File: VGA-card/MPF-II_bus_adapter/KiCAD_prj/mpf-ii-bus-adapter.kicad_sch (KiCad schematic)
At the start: 4 parts, among them J1 Bus_Apple_II_Card_Side, J2 Bus_Apple_II_Computer_Side, J3 DEVSEL_sel

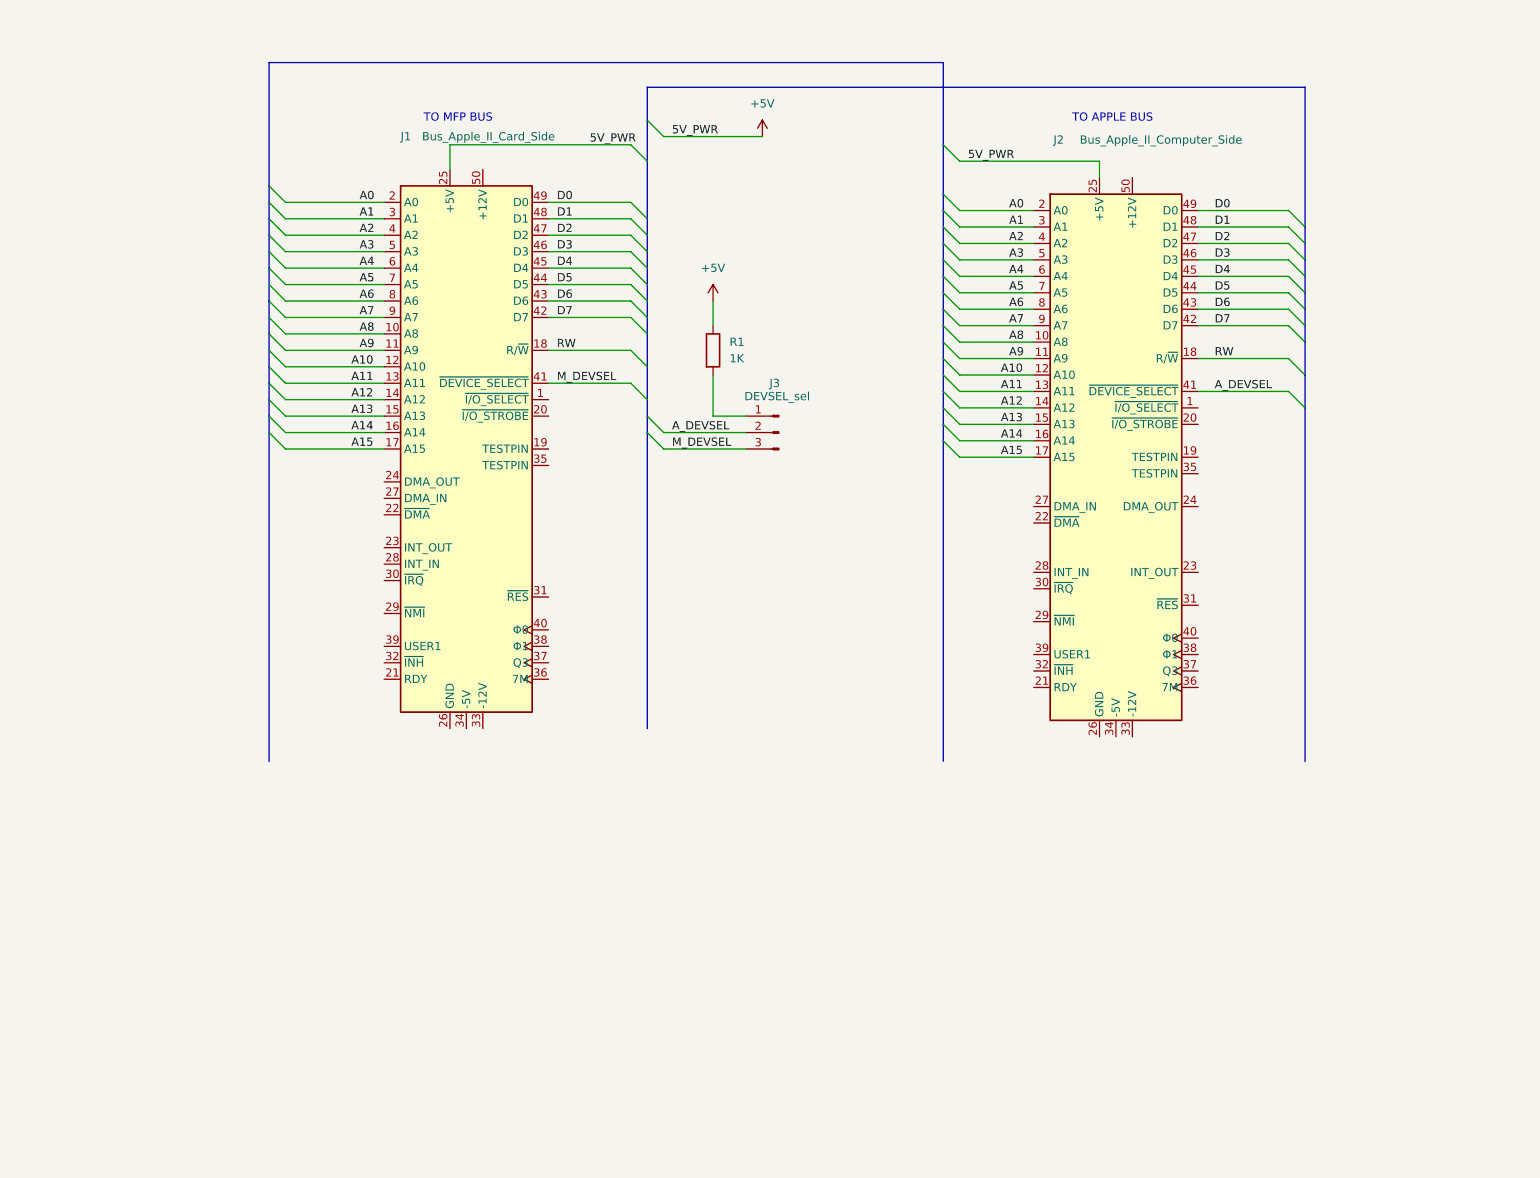
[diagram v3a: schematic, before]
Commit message: Clock signals added
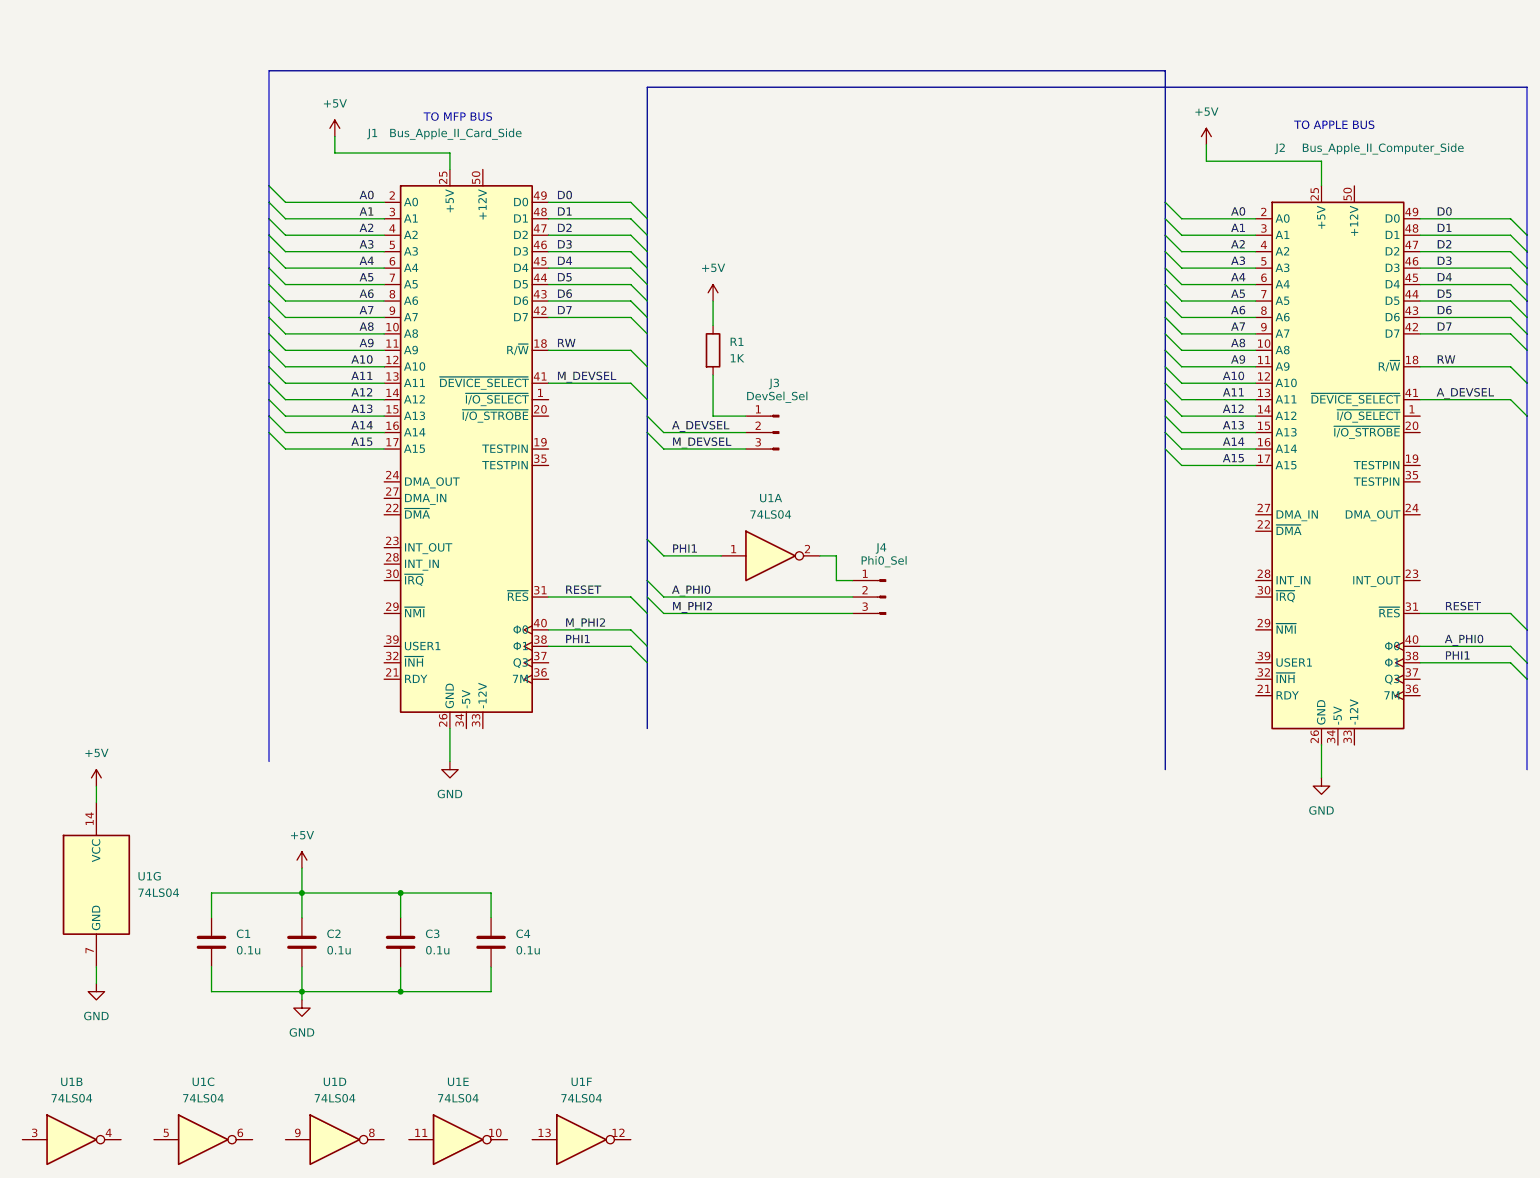
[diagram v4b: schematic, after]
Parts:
- added C1, C2, C3, C4: 0.1u, Capacitor_THT:C_Disc_D4.3mm_W1.9mm_P5.00mm, symbol Device:C
- added J4: Phi0_Sel, Connector_PinHeader_2.54mm:PinHeader_1x03_P2.54mm_Vertical, symbol Connector:Conn_01x03_Pin
- added U1: 74LS04, Package_DIP:DIP-14_W7.62mm, symbol 74xx:74LS04
- J3: value DEVSEL_sel -> DevSel_Sel
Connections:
- net +5V: now also C1.1, C2.1, C3.1, C4.1, U1.14 (VCC)
- net GND: now reaches J2.26 (GND)
- net GND: now also J1.26 (GND), C1.2, C2.2, C3.2, C4.2, U1.7 (GND)
- net RESET: now reaches J2.31 (~{RES})
- net RESET: now also J1.31 (~{RES})
- net PHI1: now reaches J2.38 (Φ1)
- net PHI1: now also J1.38 (Φ1), U1.1
- net A_PHI0: now reaches J2.40 (Φ0)
- net A_PHI0: now also J4.2 (Pin_2)
- net M_PHI2: now reaches J1.40 (Φ0)
- net M_PHI2: now also J4.3 (Pin_3)
- new net: J4.1 (Pin_1), U1.2
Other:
- moved on the sheet: J2

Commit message: Schematics updated
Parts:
- added J5: -12V_Selection, Connector_PinHeader_2.54mm:PinHeader_1x02_P2.54mm_Vertical, symbol Connector:Conn_01x02_Pin
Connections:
- net -12V: now reaches J2.33 (-12V)
- net -12V: now also J5.2 (Pin_2)
- net -5V: now reaches J2.34 (-5V)
- net -5V: now also J1.34 (-5V)
- net +12V: now reaches J2.50 (+12V)
- net +12V: now also J1.50 (+12V)
- net at J1.33 (-12V): now also J5.1 (Pin_1)

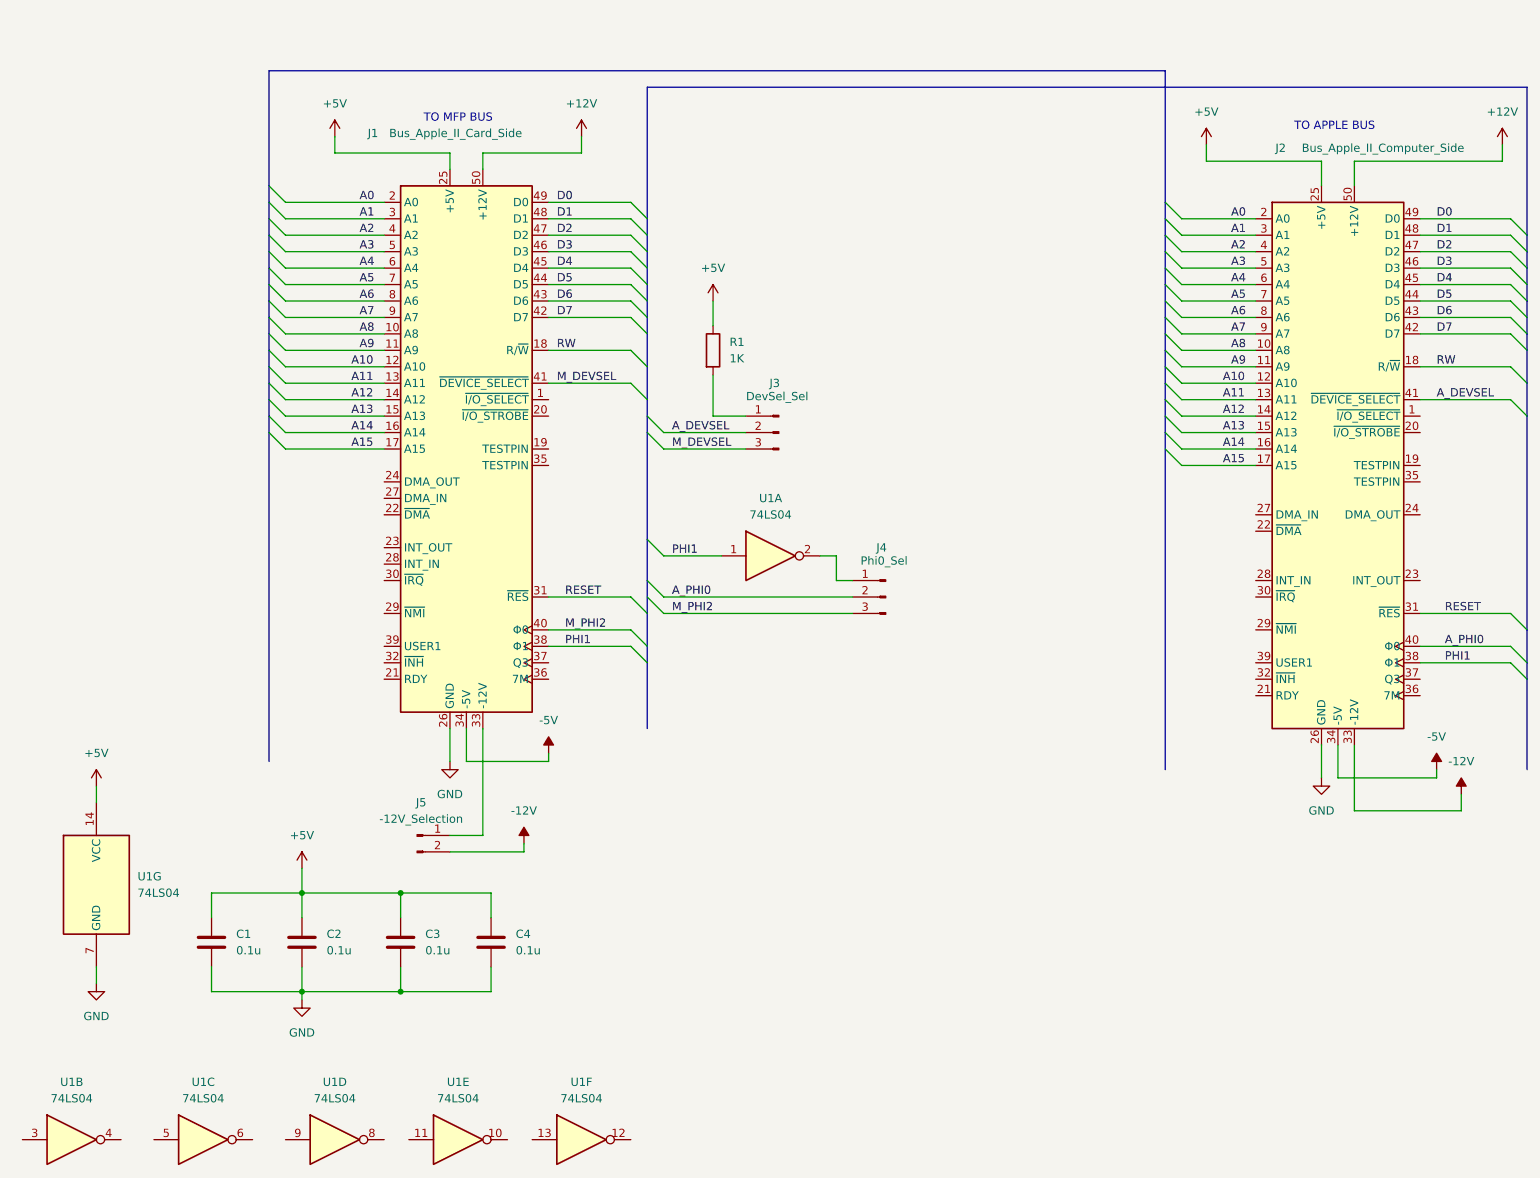
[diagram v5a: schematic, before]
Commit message: KiCAD schematics updated
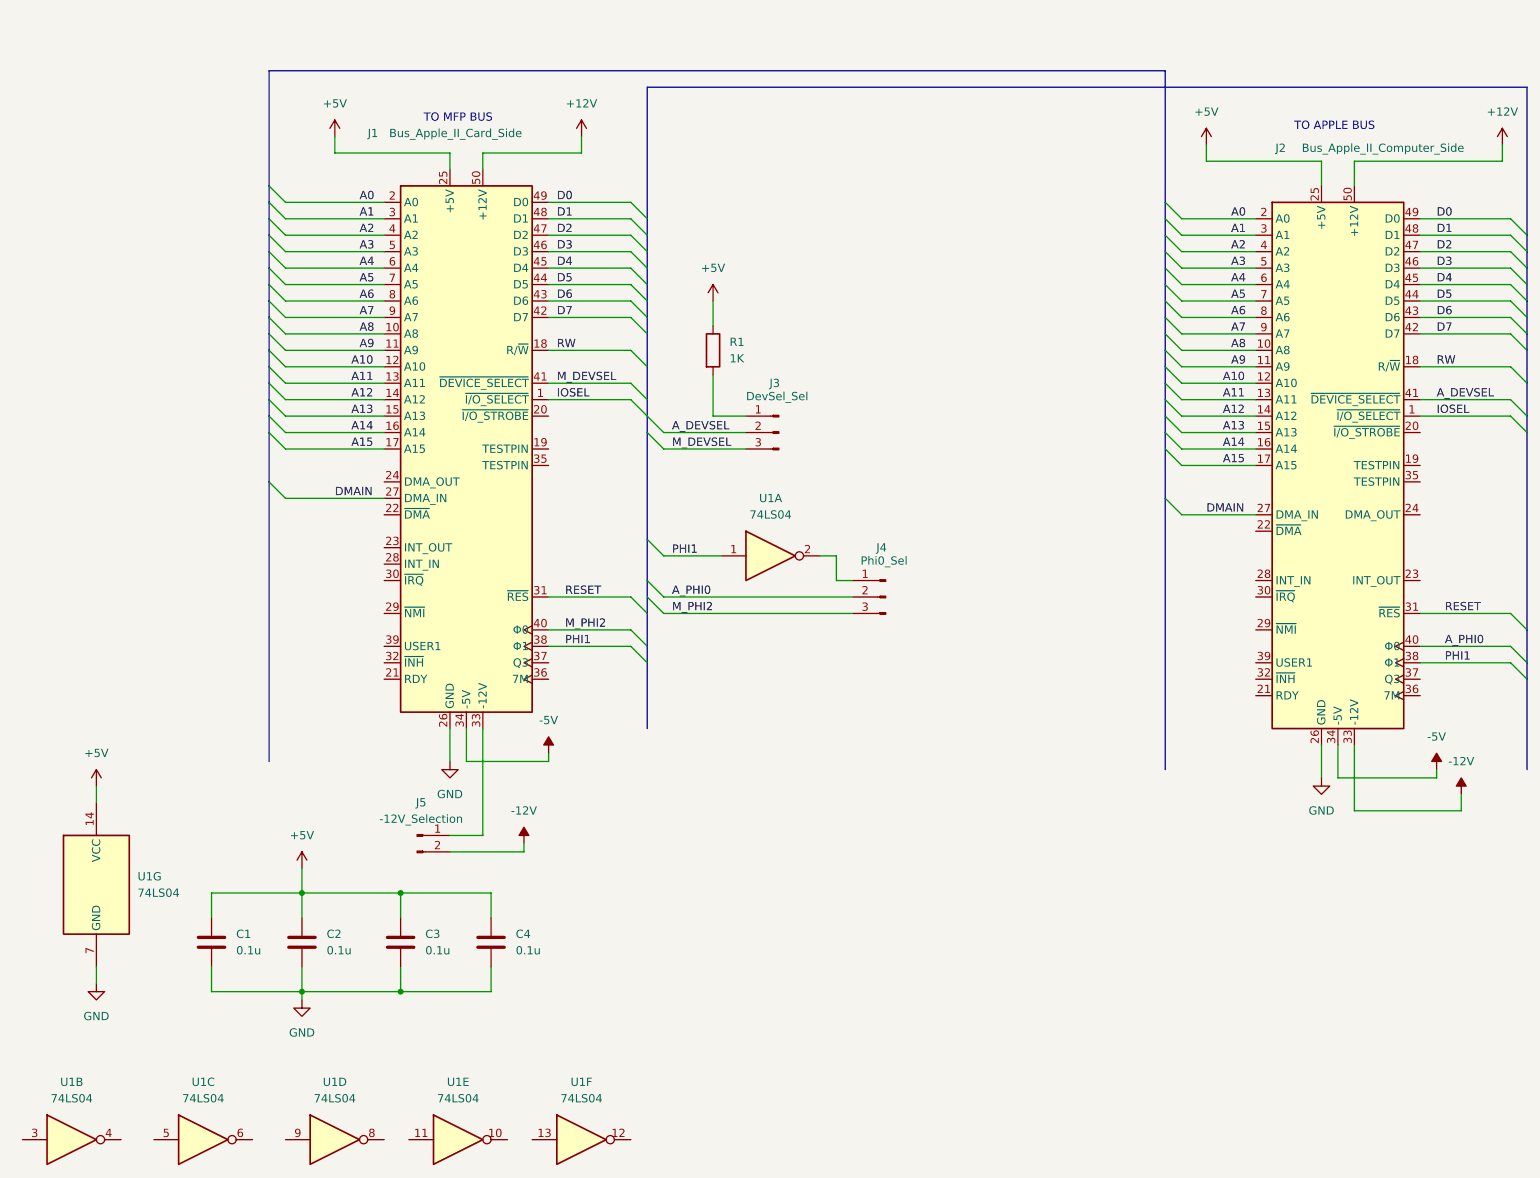
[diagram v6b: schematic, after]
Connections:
- net IOSEL: now reaches J2.1 (~{I/O_SELECT})
- net IOSEL: now also J1.1 (~{I/O_SELECT})
- net DMAIN: now reaches J2.27 (DMA_IN)
- net DMAIN: now also J1.27 (DMA_IN)
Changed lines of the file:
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@@
 	(title_block
 		(title "Microprofessor-II Bus Adapter Board")
-		(date "2024-07-19")
+		(date "2024-07-20")
 		(rev "0.1")
 		(comment 1 "Licensed under CERN-OHL-P V2.0 (https://ohwr.org/cern_ohl_p_v2.txt)")
@@
 	)
 	(bus_entry
+		(at 53.34 85.09)
+		(size 2.54 2.54)
+		(stroke
+			(width 0)
+			(type default)
+		)
+	)
+	(bus_entry
 		(at 53.34 44.45)
 		(size 2.54 2.54)
@@
 	)
 	(bus_entry
+		(at 191.77 87.63)
+		(size 2.54 2.54)
+		(stroke
+			(width 0)
+			(type default)
+		)
+	)
+	(bus_entry
 		(at 53.34 77.47)
 		(size 2.54 2.54)
@@
 	)
 	(bus_entry
+		(at 109.22 72.39)
+		(size 2.54 2.54)
+		(stroke
+			(width 0)
+			(type default)
+		)
+	)
+	(bus_entry
 		(at 53.34 67.31)
 		(size 2.54 2.54)
@@
 	)
 	(bus_entry
+		(at 245.11 74.93)
+		(size 2.54 2.54)
+		(stroke
+			(width 0)
+			(type default)
+		)
+	)
+	(bus_entry
 		(at 53.34 49.53)
 		(size 2.54 2.54)
@@
 	(bus
 		(pts
-			(xy 53.34 77.47) (xy 53.34 128.27)
+			(xy 53.34 77.47) (xy 53.34 85.09)
 		)
 		(stroke
@@
 		)
 	)
+	(bus
+		(pts
+			(xy 191.77 87.63) (xy 191.77 129.54)
+		)
+		(stroke
+			(width 0)
+			(type default)
+		)
+	)
 	(wire
 		(pts
@@
 		)
 	)
+	(wire
+		(pts
+			(xy 55.88 87.63) (xy 71.12 87.63)
+		)
+		(stroke
+			(width 0)
+			(type default)
+		)
+	)
 	(bus
 		(pts
@@
 	(wire
 		(pts
+			(xy 231.14 74.93) (xy 245.11 74.93)
+		)
+		(stroke
+			(width 0)
+			(type default)
+		)
+	)
+	(wire
+		(pts
 			(xy 44.45 148.59) (xy 58.42 148.59)
 		)
@@
 	(bus
 		(pts
-			(xy 191.77 80.01) (xy 191.77 129.54)
+			(xy 191.77 80.01) (xy 191.77 87.63)
 		)
 		(stroke
@@
 		)
 	)
+	(bus
+		(pts
+			(xy 247.65 77.47) (xy 247.65 107.95)
+		)
+		(stroke
+			(width 0)
+			(type default)
+		)
+	)
 	(wire
 		(pts
@@
 		)
 	)
+	(bus
+		(pts
+			(xy 53.34 85.09) (xy 53.34 128.27)
+		)
+		(stroke
+			(width 0)
+			(type default)
+		)
+	)
 	(wire
 		(pts
@@
 	(wire
 		(pts
+			(xy 96.52 72.39) (xy 109.22 72.39)
+		)
+		(stroke
+			(width 0)
+			(type default)
+		)
+	)
+	(wire
+		(pts
 			(xy 58.42 148.59) (xy 58.42 152.4)
 		)
@@
 	(wire
 		(pts
+			(xy 194.31 90.17) (xy 205.74 90.17)
+		)
+		(stroke
+			(width 0)
+			(type default)
+		)
+	)
+	(wire
+		(pts
 			(xy 194.31 82.55) (xy 205.74 82.55)
 		)
@@
 	(bus
 		(pts
-			(xy 247.65 74.93) (xy 247.65 107.95)
+			(xy 247.65 74.93) (xy 247.65 77.47)
 		)
 		(stroke
@@
 		)
 	)
+	(label "DMAIN"
+		(at 198.12 90.17 0)
+		(fields_autoplaced yes)
+		(effects
+			(font
+				(size 1.27 1.27)
+			)
+			(justify left bottom)
+		)
+	)
 	(label "A13"
 		(at 200.66 77.47 0)
@@
 		)
 	)
+	(label "DMAIN"
+		(at 63.5 87.63 0)
+		(fields_autoplaced yes)
+		(effects
+			(font
+				(size 1.27 1.27)
+			)
+			(justify left bottom)
+		)
+	)
 	(label "D0"
 		(at 97.79 41.91 0)
@@
 		)
 	)
+	(label "IOSEL"
+		(at 97.79 72.39 0)
+		(fields_autoplaced yes)
+		(effects
+			(font
+				(size 1.27 1.27)
+			)
+			(justify left bottom)
+		)
+	)
 	(label "M_PHI2"
 		(at 115.57 105.41 0)
@@
 		(fields_autoplaced yes)
 		(effects
+			(font
+				(size 1.27 1.27)
+			)
+			(justify left bottom)
+		)
+	)
+	(label "IOSEL"
+		(at 233.68 74.93 0)
+		(fields_autoplaced yes)
+		(effects
